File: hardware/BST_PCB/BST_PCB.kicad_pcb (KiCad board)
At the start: 2 copper layers, 106.5 x 106.5 mm, 14 parts

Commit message: Merging into pull request
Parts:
- added Supercap1: ~, components:Supercap, F.Cu at (146.9, 92.5)
- added Supercap2: ~, components:Supercap, F.Cu at (146.9, 100.5)
- Supercap reserve: renamed from Supercap1
- moved Pololu 2.00 mm to (151.2, 123.5)
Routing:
- net VBAT: track 28.4 -> 25.5 mm
- net GND: track 248.1 -> 245.6 mm
- net 5v: track 252.0 -> 251.0 mm
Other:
- board text added: "OLB BST PCB V2.1 If found, contact larswd@proton.me"
- board text removed: "OLB BST PCB V2 If found, contact larswd@proton.me"

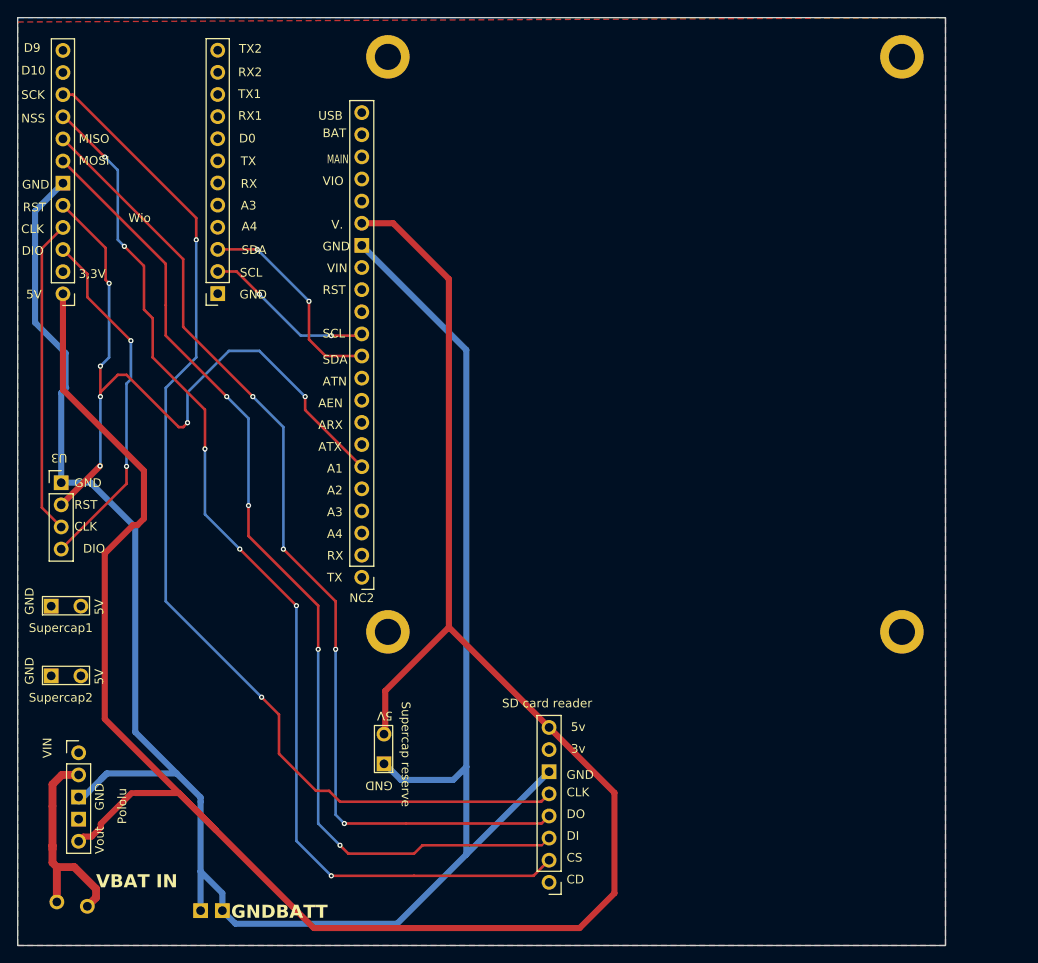
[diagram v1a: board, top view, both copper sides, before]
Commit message: Added more documentation, fixed BST PCB
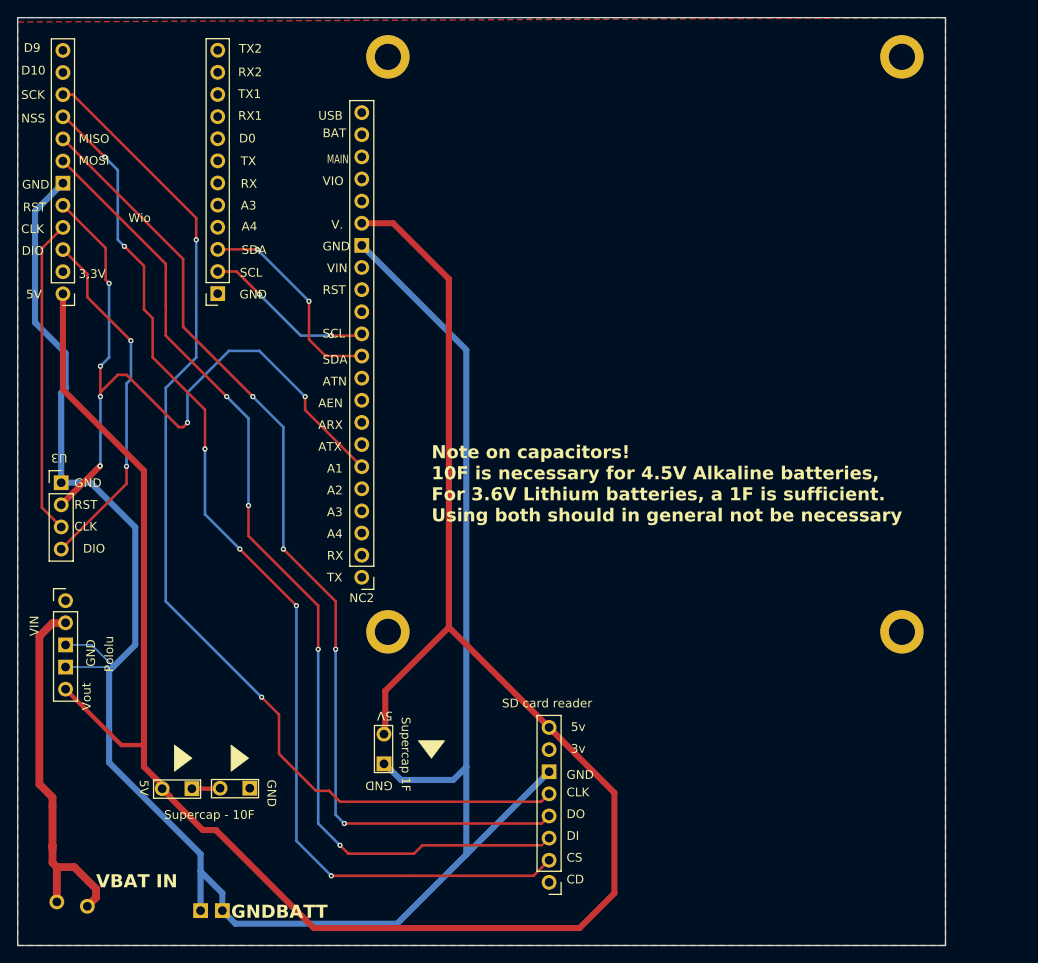
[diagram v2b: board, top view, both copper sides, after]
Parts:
- Supercap - 10F: renamed from Supercap1
- Supercap 1F: renamed from Supercap reserve
- moved Supercap - 10F 32.3 mm to (171.6, 113.5), turned to -90 degrees
- moved Supercap2 22.1 mm to (164.9, 113.5), turned to -90 degrees
- moved Pololu 17.5 mm to (149.7, 106.0)
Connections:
- Supercap - 10F pad 5V: (no net) -> unconnected-(U1-3,3V-Pad3V)
- Supercap2 pad 5V: (no net) -> 5v
- Supercap2 pad vout: GND -> unconnected-(U1-3,3V-Pad3V)
- Wio pad 3V: unconnected-(U1-3,3V-Pad3V) -> (no net)
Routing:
- net VBAT: track 25.5 -> 43.3 mm
- net 5v: track 251.0 -> 239.1 mm
- net GND: track 245.6 -> 250.4 mm
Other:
- board text added: "Note on capacitors! 10F is necessary for 4.5V Alkaline batteries, For 3.6V Lithium batteries, a 1F is sufficient. Using both should in general not be necessary"
- board text added: "OLB BST PCB V2.2 If found, contact larswd@proton.me"
- board text removed: "OLB BST PCB V2.1 If found, contact larswd@proton.me"
